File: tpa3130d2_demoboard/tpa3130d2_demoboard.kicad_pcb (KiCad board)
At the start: 2 copper layers, 5 parts, among them J1 AudioJack3_Ground_SwitchTR, J2 Conn_01x03_Pin, J3 Screw_Terminal_01x02, J4 Barrel_Jack_MountingPin, U1 TPA3130D2DAPR

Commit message: Fill BOM
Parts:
- removed J1: AudioJack3_Ground_SwitchTR, tpa3130d2_demoboard:AudioJack_3.5mm_PJ311
- removed J2: Conn_01x03_Pin, Connector_PinHeader_2.54mm:PinHeader_1x03_P2.54mm_Vertical
- removed J3: Screw_Terminal_01x02, TerminalBlock:TerminalBlock_bornier-2_P5.08mm
- removed J4: Barrel_Jack_MountingPin, Connector_BarrelJack:BarrelJack_GCT_DCJ200-10-A_Horizontal
- removed U1: TPA3130D2DAPR, tpa3130d2_demoboard:TPA3130D2DAPR_M
- added C100: 1uF, Capacitor_Tantalum_SMD:CP_EIA-3216-18_Kemet-A, F.Cu at (144.3, 71.7)
- added C101: 1uF, Capacitor_Tantalum_SMD:CP_EIA-3216-18_Kemet-A, F.Cu at (144.3, 74.9)
- added C102: 1uF, Capacitor_Tantalum_SMD:CP_EIA-3216-18_Kemet-A, F.Cu at (144.3, 78.0)
- added C103: 1uF, Capacitor_Tantalum_SMD:CP_EIA-3216-18_Kemet-A, F.Cu at (144.3, 81.2)
- added C200: 220uF, Capacitor_THT:CP_Radial_D6.3mm_P2.50mm, F.Cu at (138.0, 43.3)
- added C201: 220uF, Capacitor_THT:CP_Radial_D6.3mm_P2.50mm, F.Cu at (138.0, 51.2)
- added C202: 220nF, Capacitor_SMD:C_0603_1608Metric, F.Cu at (133.2, 40.7)
- added C203: 220nF, Capacitor_SMD:C_0603_1608Metric, F.Cu at (133.2, 43.2)
- added C204: 220nF, Capacitor_SMD:C_0603_1608Metric, F.Cu at (133.2, 45.7)
- added C205: 220nF, Capacitor_SMD:C_0603_1608Metric, F.Cu at (133.2, 48.2)
- added C206: 220nF, Capacitor_SMD:C_0603_1608Metric, F.Cu at (133.2, 50.7)
- added C207: 1uF, Capacitor_Tantalum_SMD:CP_EIA-3216-18_Kemet-A, F.Cu at (127.7, 57.7)
- added C300: 220nF, Capacitor_SMD:C_0603_1608Metric, F.Cu at (101.6, 58.8)
- added C301: 220nF, Capacitor_SMD:C_0603_1608Metric, F.Cu at (101.6, 61.3)
- added C302: 1uF, Capacitor_Tantalum_SMD:CP_EIA-3216-18_Kemet-A, F.Cu at (114.0, 41.0)
- added C303: 1uF, Capacitor_Tantalum_SMD:CP_EIA-3216-18_Kemet-A, F.Cu at (114.0, 44.1)
- added C304: 1nF, Capacitor_SMD:C_0603_1608Metric, F.Cu at (101.6, 63.8)
- added C305: 1nF, Capacitor_SMD:C_0603_1608Metric, F.Cu at (101.6, 66.3)
- added C306: 10nF, Capacitor_SMD:C_0603_1608Metric, F.Cu at (101.6, 68.8)
- added C307: 10nF, Capacitor_SMD:C_0603_1608Metric, F.Cu at (105.6, 58.8)
- added C308: 220nF, Capacitor_SMD:C_0603_1608Metric, F.Cu at (105.6, 61.3)
- added C309: 220nF, Capacitor_SMD:C_0603_1608Metric, F.Cu at (105.6, 63.8)
- added C310: 1uF, Capacitor_Tantalum_SMD:CP_EIA-3216-18_Kemet-A, F.Cu at (114.0, 47.3)
- added C311: 1uF, Capacitor_Tantalum_SMD:CP_EIA-3216-18_Kemet-A, F.Cu at (114.0, 50.4)
- added C312: 1nF, Capacitor_SMD:C_0603_1608Metric, F.Cu at (105.6, 66.3)
- added C313: 1nF, Capacitor_SMD:C_0603_1608Metric, F.Cu at (105.6, 68.8)
- added C314: 10nF, Capacitor_SMD:C_0603_1608Metric, F.Cu at (109.6, 58.8)
- added C315: 10nF, Capacitor_SMD:C_0603_1608Metric, F.Cu at (109.6, 61.3)
- added D200: D, Diode_SMD:D_PowerDI-123, F.Cu at (121.8, 58.0)
- added J100: Screw_Terminal_01x02, TerminalBlock:TerminalBlock_bornier-2_P5.08mm, F.Cu at (122.1, 74.7)
- added J101: AudioJack3_Ground_SwitchTR, tpa3130d2_demoboard:AudioJack_3.5mm_PJ311, F.Cu at (135.9, 75.0)
- added J102: Screw_Terminal_01x02, TerminalBlock:TerminalBlock_bornier-2_P5.08mm, F.Cu at (122.1, 83.7)
- added J200: Barrel_Jack_MountingPin, Connector_BarrelJack:BarrelJack_GCT_DCJ200-10-A_Horizontal, F.Cu at (124.3, 41.4)
- added J300: Screw_Terminal_01x02, TerminalBlock:TerminalBlock_bornier-2_P5.08mm, F.Cu at (102.8, 43.9)
- added J301: Screw_Terminal_01x02, TerminalBlock:TerminalBlock_bornier-2_P5.08mm, F.Cu at (102.8, 53.0)
- added L300: 10uH, Inductor_SMD:L_Wuerth_HCM-7050, F.Cu at (95.1, 43.8)
- added L301: 10uH, Inductor_SMD:L_Wuerth_HCM-7050, F.Cu at (95.1, 52.5)
- added L302: 10uH, Inductor_SMD:L_Wuerth_HCM-7050, F.Cu at (95.1, 61.3)
- added L303: 10uH, Inductor_SMD:L_Wuerth_HCM-7050, F.Cu at (95.1, 70.0)
- added R100: 47kR, Resistor_SMD:R_0603_1608Metric, F.Cu at (143.4, 84.0)
- added R101: 47kR, Resistor_SMD:R_0603_1608Metric, F.Cu at (143.4, 86.5)
- added R200: DNP, Resistor_SMD:R_0603_1608Metric, F.Cu at (133.2, 53.2)
- added R201: 5kR6, Resistor_SMD:R_0603_1608Metric, F.Cu at (133.2, 55.7)
- added R202: 47kR, Resistor_SMD:R_0603_1608Metric, F.Cu at (133.2, 58.2)
- added R203: 47kR, Resistor_SMD:R_0603_1608Metric, F.Cu at (133.2, 60.7)
- added R302: 47kR, Resistor_SMD:R_0603_1608Metric, F.Cu at (109.6, 63.8)
- added R305: 47kR, Resistor_SMD:R_0603_1608Metric, F.Cu at (109.6, 66.3)
- added U200: TPA3130D2DAPR, tpa3130d2_demoboard:TPA3130D2DAPR_M, F.Cu at (140.2, 62.0)

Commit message: Footprint updates
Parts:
- added R300: 3R3, Resistor_SMD:R_0603_1608Metric, F.Cu at (155.7, 44.2)
- added R301: 3R3, Resistor_SMD:R_0603_1608Metric, F.Cu at (155.7, 46.7)
- added R303: 3R3, Resistor_SMD:R_0603_1608Metric, F.Cu at (155.7, 49.2)
- added R304: 3R3, Resistor_SMD:R_0603_1608Metric, F.Cu at (155.7, 51.8)
- L300, L301, L302, L303: footprint Inductor_SMD:L_Wuerth_HCM-7050 -> tpa3130d2_demoboard:Inductor_CYA0630-10UH

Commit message: Initial PCB layout
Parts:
- added H1: MountingHole, MountingHole:MountingHole_3.2mm_M3, F.Cu at (60.2, 70.0)
- added H2: MountingHole, MountingHole:MountingHole_3.2mm_M3, F.Cu at (125.2, 70.0)
- added H3: MountingHole, MountingHole:MountingHole_3.2mm_M3, F.Cu at (125.0, 115.0)
- added H4: MountingHole, MountingHole:MountingHole_3.2mm_M3, F.Cu at (60.2, 115.0)
- moved J101 78.1 mm to (59.8, 92.5), turned to 90 degrees
- moved R101 70.7 mm to (73.5, 97.0), turned to -90 degrees
- moved R100 70.0 mm to (73.5, 87.7), turned to -90 degrees
- moved C201 69.8 mm to (91.8, 103.5), turned to 180 degrees
- moved C102 69.7 mm to (76.9, 95.7), turned to 180 degrees
- moved C103 69.5 mm to (76.9, 98.2), turned to 180 degrees
- moved C100 69.0 mm to (76.9, 86.5), turned to 180 degrees
- moved C101 68.8 mm to (76.9, 89.0), turned to 180 degrees
- moved R303 68.0 mm to (115.2, 104.0), turned to 90 degrees
- moved R201 65.9 mm to (77.6, 91.2), turned to 180 degrees
- moved J102 65.2 mm to (59.5, 102.2), turned to -90 degrees
- moved R200 64.7 mm to (80.8, 91.2), turned to 180 degrees
- moved C204 62.8 mm to (98.0, 97.7)
- moved J100 62.6 mm to (59.5, 77.7), turned to -90 degrees
- moved R203 62.4 mm to (84.0, 99.2), turned to -90 degrees
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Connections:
- J301 pad 1: /audio_output/OUT_L_P -> /audio_output/OUT_L_N
- J301 pad 2: /audio_output/OUT_L_N -> /audio_output/OUT_L_P
- U200 pad 17: GND -> +15V
- U200 pad 18: GND -> +15V
- U200 pad 19: GND -> +15V
- U200 pad 31: GND -> +15V
- U200 pad 32: GND -> +15V
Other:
- board outline added: 75 x 55 mm
- rule pad_to_mask_clearance: 0 -> 0.038

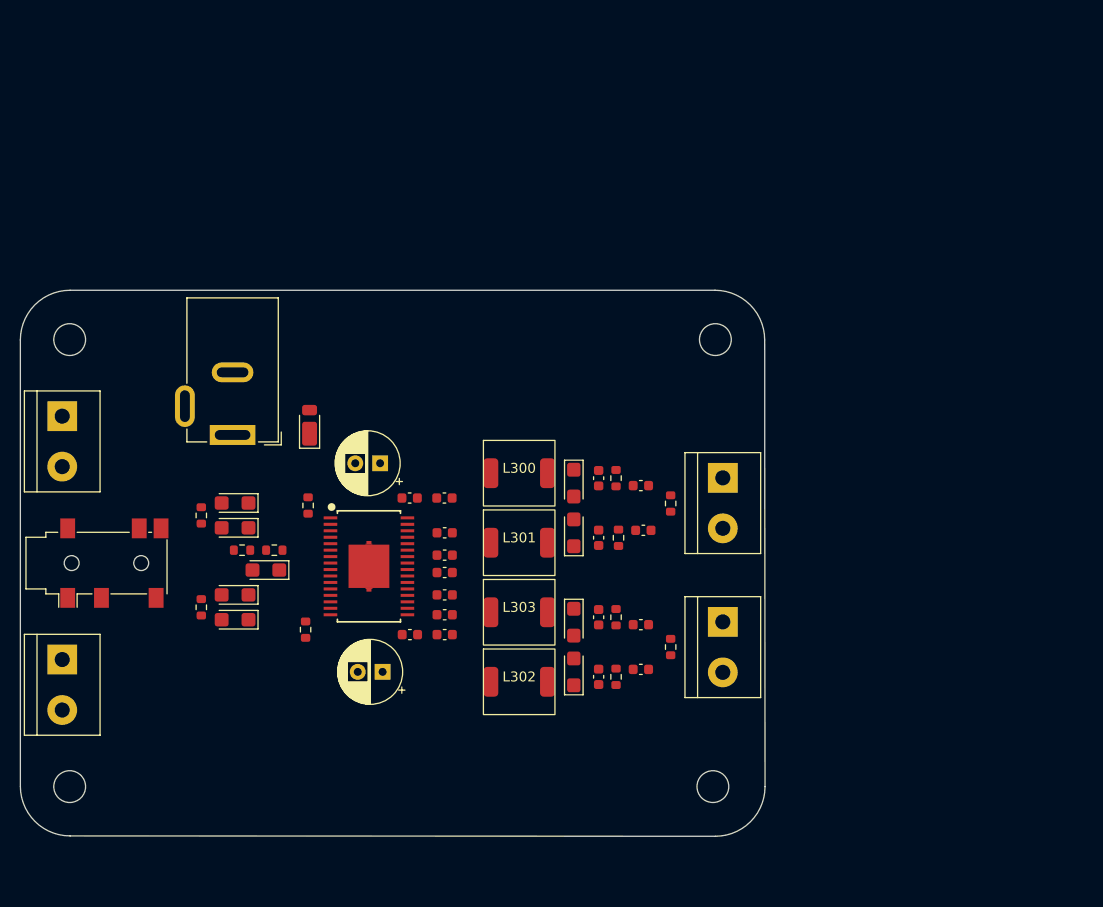
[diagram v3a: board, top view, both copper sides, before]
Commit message: Minor changes in terminal block footprint
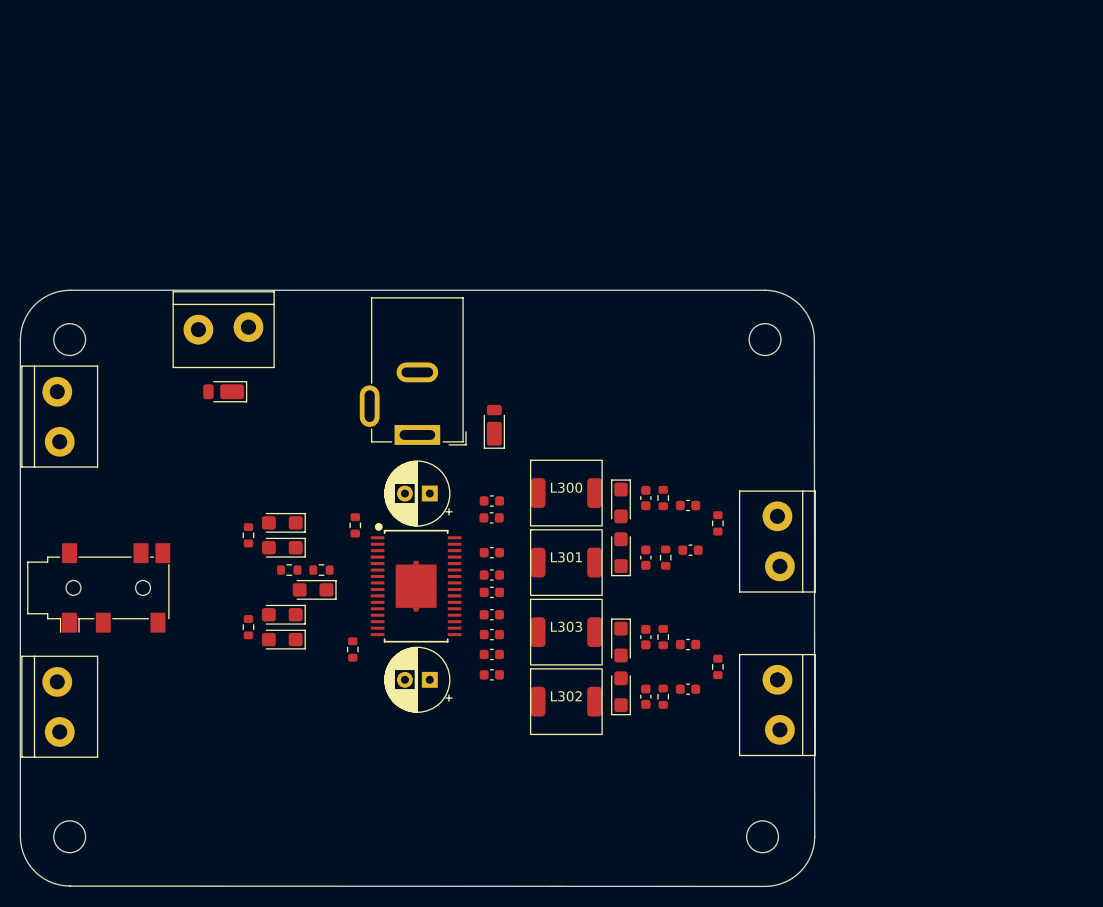
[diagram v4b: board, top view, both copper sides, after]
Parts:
- added D201: D, Diode_SMD:D_PowerDI-123, F.Cu at (75.8, 75.2)
- added J201: Screw_Terminal_01x02, tpa3130d2_demoboard:terminal_block, F.Cu at (75.8, 69.2)
- J100, J102, J300, J301: footprint TerminalBlock:TerminalBlock_bornier-2_P5.08mm -> tpa3130d2_demoboard:terminal_block
- moved D200 18.6 mm to (103.0, 78.6)
- moved J200 18.6 mm to (95.2, 79.6)
- moved J301 9.88 mm to (131.2, 106.8), turned to 90 degrees
- moved C206 9.19 mm to (102.8, 103.8)
- moved J300 8.29 mm to (131.2, 90.3), turned to 90 degrees
- moved C202 8.28 mm to (102.8, 86.2), turned to 0 degrees
- moved H3 7.11 mm to (130.0, 120.0)
- moved C200 5.86 mm to (96.5, 85.5)
- moved C100 5.15 mm to (81.7, 88.5)
- moved C101 5.15 mm to (81.7, 91.0)
- moved C102 5.15 mm to (81.7, 97.7)
- moved C103 5.15 mm to (81.7, 100.2)
- moved C203 5.15 mm to (102.7, 88.0)
- moved C204 5.15 mm to (102.8, 99.7)
- moved C205 5.15 mm to (102.8, 101.7)
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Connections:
- J102 pad 1: GND -> /audio_input/IN_L
- J102 pad 2: /audio_input/IN_L -> GND
- J300 pad 1: /audio_output/OUT_R_P -> /audio_output/OUT_R_N
- J300 pad 2: /audio_output/OUT_R_N -> /audio_output/OUT_R_P
- J301 pad 1: /audio_output/OUT_L_N -> /audio_output/OUT_L_P
- J301 pad 2: /audio_output/OUT_L_P -> /audio_output/OUT_L_N
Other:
- board size 75 x 55 mm -> 80 x 60 mm

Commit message: Initial PCB routing
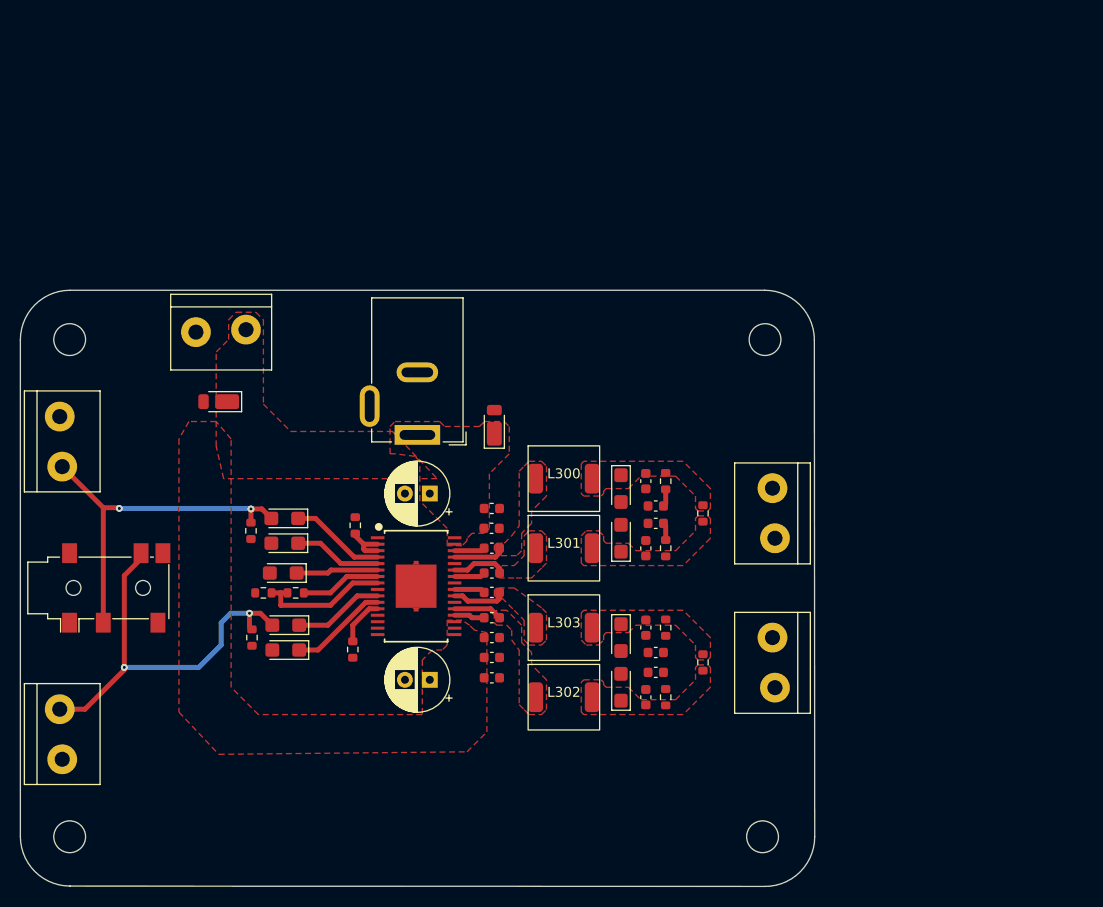
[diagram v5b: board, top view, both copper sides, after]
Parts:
- moved C307 4.42 mm to (119.2, 88.5), turned to 180 degrees
- moved J301 4.28 mm to (130.8, 102.5)
- moved C314 3.67 mm to (119.2, 103.5), turned to 180 degrees
- moved R200 3.47 mm to (83.0, 95.5)
- moved R201 3.47 mm to (79.8, 95.5)
- moved C207 3.45 mm to (81.8, 93.5)
- moved C315 3.35 mm to (119.2, 101.5), turned to 180 degrees
- moved C306 3.25 mm to (119.2, 86.8), turned to 180 degrees
- moved J300 2.87 mm to (130.8, 87.5)
- moved J102 2.76 mm to (59.8, 109.7)
- moved J100 2.51 mm to (59.8, 80.2)
- moved R302 1.80 mm to (124.0, 87.5)
- moved R300 1.72 mm to (120.2, 84.2)
- moved C304 1.70 mm to (118.2, 84.2)
- moved R305 1.57 mm to (124.0, 102.5)
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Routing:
- net /audio_input/IN_L: track 0.00 -> 41.3 mm, vias 0 -> 2
- net /audio_input/IN_R: track 0.00 -> 36.2 mm, vias 0 -> 2
- net Net-(U200-GVDD): track 0.00 -> 16.4 mm
- net Net-(U200-GAIN_SLV): track 0.00 -> 13.5 mm
- net LINN: track 0.00 -> 9.89 mm
- net RINP: track 0.00 -> 9.62 mm
- net LINP: track 0.00 -> 9.12 mm
- net RINN: track 0.00 -> 8.85 mm
- net OUTNR: track 0.00 -> 5.47 mm
- net OUTNL: track 0.00 -> 5.46 mm
- net OUTPR: track 0.00 -> 5.18 mm
- net OUTPL: track 0.00 -> 4.90 mm
- net /tpa3130d2/MUTE: track 0.00 -> 4.81 mm
- net Net-(U200-FAULTZ): track 0.00 -> 4.80 mm
- net BSNR: track 0.00 -> 3.12 mm
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- added copper zone on F.Cu, net +15V
- added copper zone on F.Cu, net /audio_output/OUT_L_N
- added copper zone on F.Cu, net /audio_output/OUT_L_P
- added copper zone on F.Cu, net /audio_output/OUT_R_N
- added copper zone on F.Cu, net /audio_output/OUT_R_P
- added copper zone on F.Cu, net OUTNL
- added copper zone on F.Cu, net OUTNR
- added copper zone on F.Cu, net OUTPL
- added copper zone on F.Cu, net OUTPR

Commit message: Copper fill updates
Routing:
- net +15V: track 0.89 -> 34.7 mm
- net /audio_input/IN_L: track 41.3 -> 37.4 mm
- net GND: vias 0 -> 8
- added copper zone on B.Cu, net GND
- added copper zone on F.Cu, net GND

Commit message: DRC fixes
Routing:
- net GND: track 0.00 -> 23.3 mm, vias 8 -> 149
- net +15V: track 34.7 -> 37.1 mm
- net Net-(U200-GVDD): track 16.4 -> 18.7 mm
- net Net-(C315-Pad1): track 0.00 -> 1.77 mm
- net Net-(C314-Pad1): track 0.00 -> 1.77 mm
